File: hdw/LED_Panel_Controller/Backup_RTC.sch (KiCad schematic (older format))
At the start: 14 parts

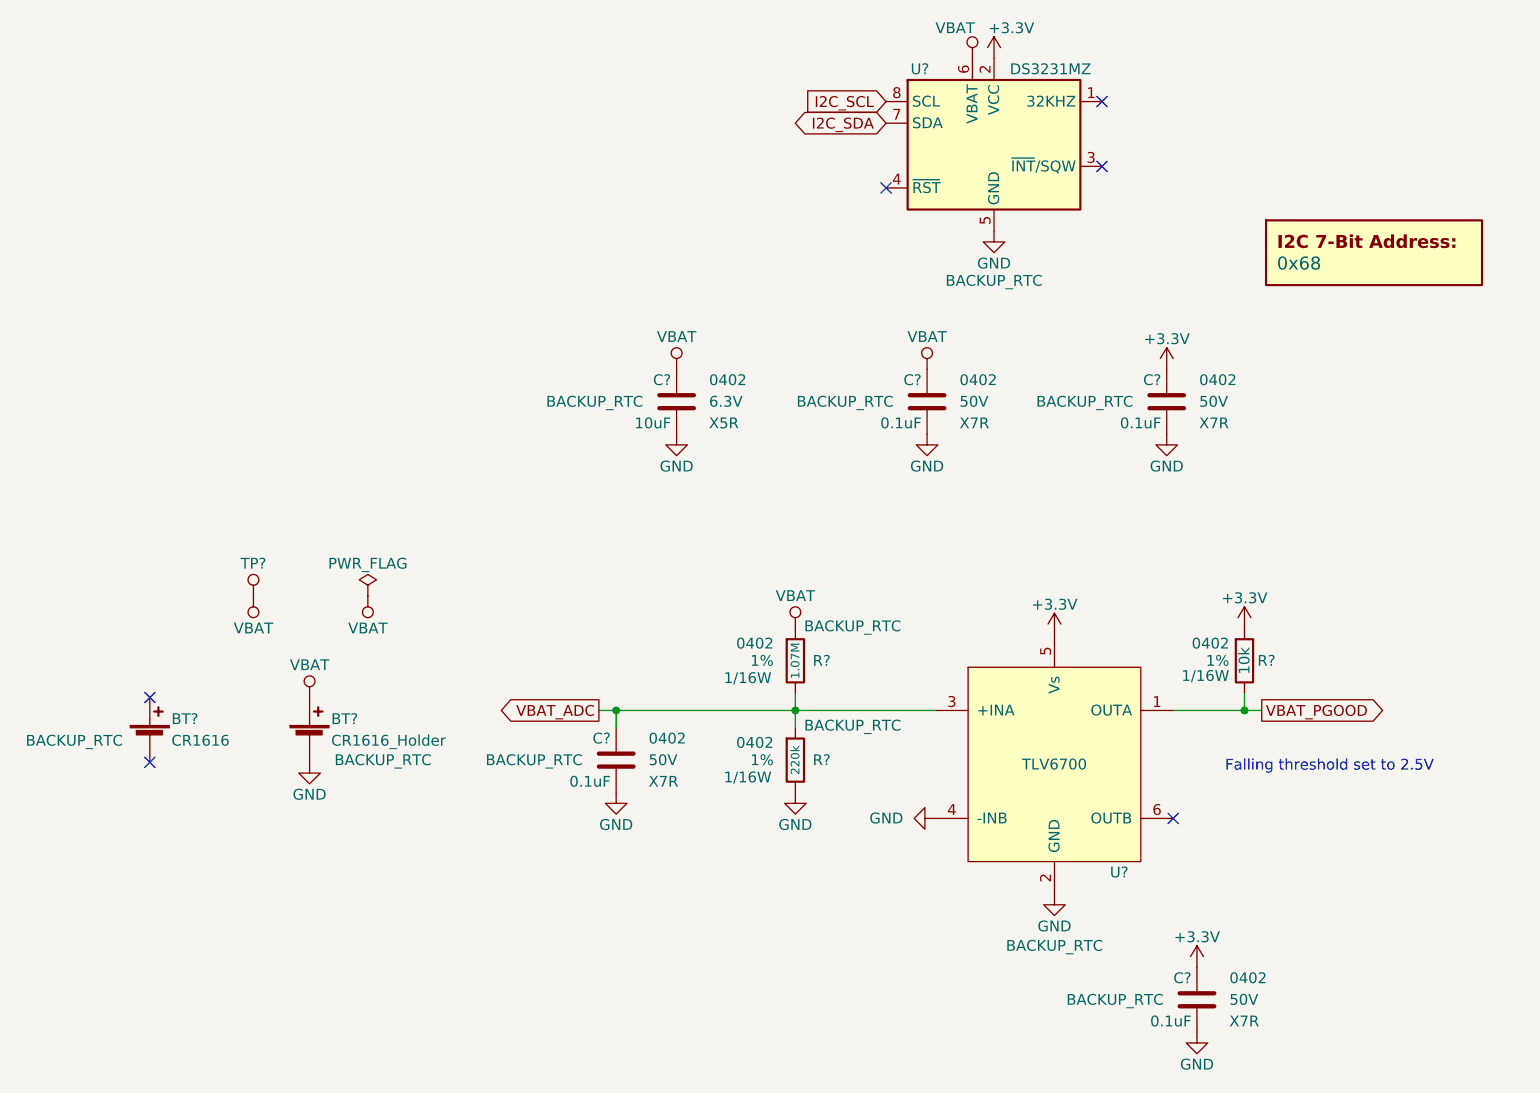
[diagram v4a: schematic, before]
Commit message: assigned I2C addresses
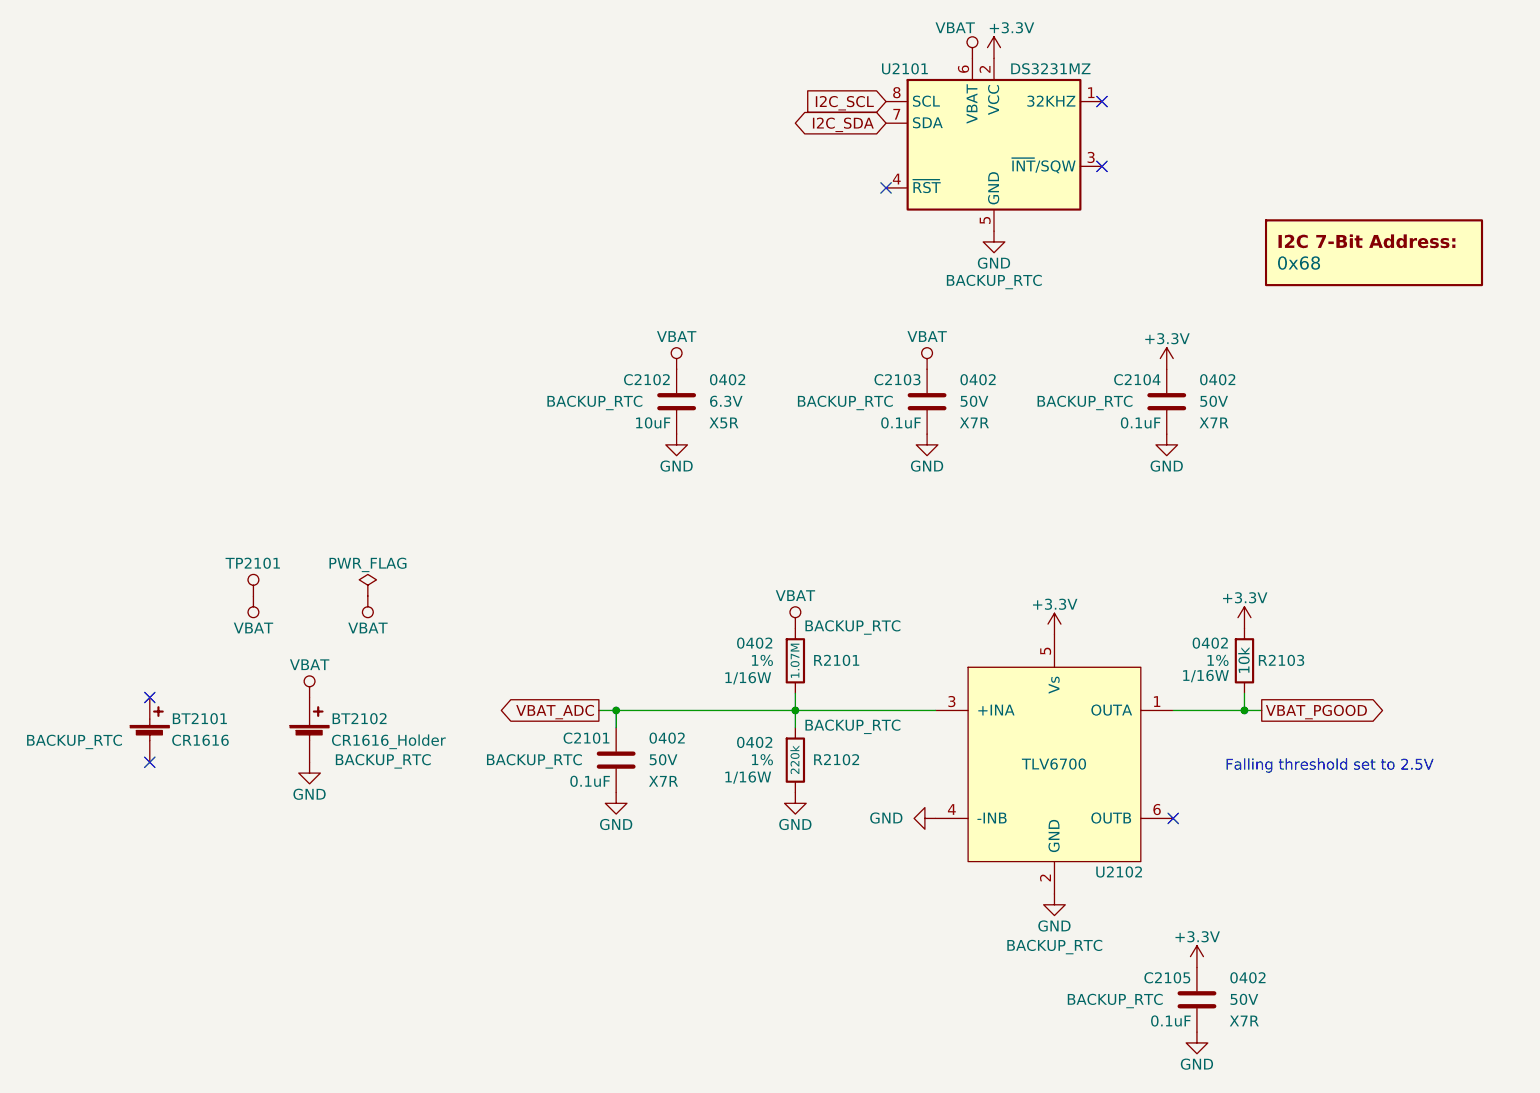
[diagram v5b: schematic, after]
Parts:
- gave numbers to parts that had none: 14

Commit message: added BOMs, some consolidation
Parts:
- C2101, C2103, C2104, C2105: Digi-Key PN 490-10701-1-ND -> 490-10698-1-ND
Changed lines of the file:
@@
 F 6 "X7R" H 3150 4750 50  0000 R CNN "Dielectric"
 F 7 "BACKUP_RTC" H 3680 4850 50  0000 C CNN "Configuration"
-F 8 "490-10701-1-ND" H 3300 4850 50  0001 C CNN "Digi-Key PN"
+F 8 "490-10698-1-ND" H 3300 4850 50  0001 C CNN "Digi-Key PN"
 	1    3300 4850
 	-1   0    0    -1
@@
 F 6 "X7R" H 5840 5860 50  0000 R CNN "Dielectric"
 F 7 "BACKUP_RTC" H 6370 5960 50  0000 C CNN "Configuration"
-F 8 "490-10701-1-ND" H 5990 5960 50  0001 C CNN "Digi-Key PN"
+F 8 "490-10698-1-ND" H 5990 5960 50  0001 C CNN "Digi-Key PN"
 	1    5990 5960
 	-1   0    0    -1
@@
 F 6 "X7R" H 5700 3090 50  0000 R CNN "Dielectric"
 F 7 "BACKUP_RTC" H 6230 3190 50  0000 C CNN "Configuration"
-F 8 "490-10701-1-ND" H 5850 3190 50  0001 C CNN "Digi-Key PN"
+F 8 "490-10698-1-ND" H 5850 3190 50  0001 C CNN "Digi-Key PN"
 	1    5850 3190
 	-1   0    0    -1
@@
 F 6 "X7R" H 4590 3090 50  0000 R CNN "Dielectric"
 F 7 "BACKUP_RTC" H 5120 3190 50  0000 C CNN "Configuration"
-F 8 "490-10701-1-ND" H 4740 3190 50  0001 C CNN "Digi-Key PN"
+F 8 "490-10698-1-ND" H 4740 3190 50  0001 C CNN "Digi-Key PN"
 	1    4740 3190
 	-1   0    0    -1
